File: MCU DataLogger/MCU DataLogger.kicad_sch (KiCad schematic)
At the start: 25 parts, among them U1 24LC1025, U2 DS1337S_, U3 ATMEGA328P-AN, U4 24LC1025, Y1 32.768 KHz, Y2 16MHz

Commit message: MCU Datalogger Project Schematic Complete
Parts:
- U3: footprint ATMEGA328P:QFP80P900X900X120-32N -> ATMEGA328P-AN:QFP80P900X900X120-32N
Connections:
- net VCC: now reaches C1.1
- net VCC: now also R1.1, R2.1, R3.1, R4.1, R6.2, U1.1 (A0), U1.2 (A1), U1.3 (A2), U1.8 (VCC), U2.8 (VCC), U4.1 (A0), U4.3 (A2), U4.8 (VCC)
- net GND: now reaches C1.2
- net GND: now also BT1.2 (-), C2.1, C3.1, C4.1, C5.2, R5.1, R7.2, U1.4 (GND), U1.7 (WP), U2.4 (GND), U3.21 (GND), U3.3 (GND), U3.5 (GND), U4.2 (A1), U4.4 (GND), U4.7 (WP)
- net D3: now reaches U3.1 (PD3)
- net D6: now reaches U3.10 (PD6)
- net D7: now reaches U3.11 (PD7)
- net D8: now reaches U3.12 (PB0)
- net MOSI: now reaches U3.15 (PB3)
- net MISO: now reaches U3.16 (PB4)
- net SCK: now reaches U3.17 (PB5)
- net SCK: now also D1.2 (A), R3.2, U1.6 (SCL), U2.6 (SCL), U3.28 (PC5), U4.6 (SCL)
- net at U3.18 (AVCC): now also BT1.1 (+), C5.1, D2.2 (A), U3.4 (VCC)
- net D4: now reaches U3.2 (PD4)
- net at U3.20 (AREF): now also C4.2
- net SDA: now reaches U3.27 (PC4)
- net SDA: now also R4.2, U1.5 (SDA), U2.5 (SDA), U4.5 (SDA)
- net RESET: now reaches U3.29 (PC6/~{RESET})
- net RESET: now also R6.1
- net RX: now reaches U3.30 (PD0)
- net TX: now reaches U3.31 (PD1)
- net D2: now reaches U3.32 (PD2)
- net at U3.6 (VCC): no longer U3.4 (VCC)
- net at U3.7 (PB6): now also C2.2, Y2.2
- net at U3.8 (PB7): now also C3.2, Y2.1
- net D5: now reaches U3.9 (PD5)
- net at D2.1 (K): now also R7.1
- net at U2.1 (X1): now also Y1.1
- net at U2.2 (X2): now also Y1.2
- net at U2.3 (~{INTA}): now also R1.2
- net at U2.7 (SQW/~INT): now also R2.2
- net at D1.1 (K): now also R5.2
- no-connect marks 0 -> 9
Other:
- sheet Connectors ports: added D2, D3, D4, D5, D6, D7, D8, GND, MISO, MOSI, RESET, RX, SCK, SDA, TX, VCC; removed none
- moved on the sheet: BT1, C1, C2, C3, C4, C5, D1, D2, H1, H2, H3, H4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

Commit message: MCU Datalogger Project 2 Layers V1 Completed
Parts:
- U3: footprint ATMEGA328P-AN:QFP80P900X900X120-32N -> ATMEGA328P:QFP80P900X900X120-32N
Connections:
- net GND: no longer U3.3 (GND), U3.5 (GND)
- net VCC: now also BT1.1 (+), C5.1, D2.2 (A), U3.18 (AVCC), U3.4 (VCC)
- new net: U3.3 (GND), U3.5 (GND)

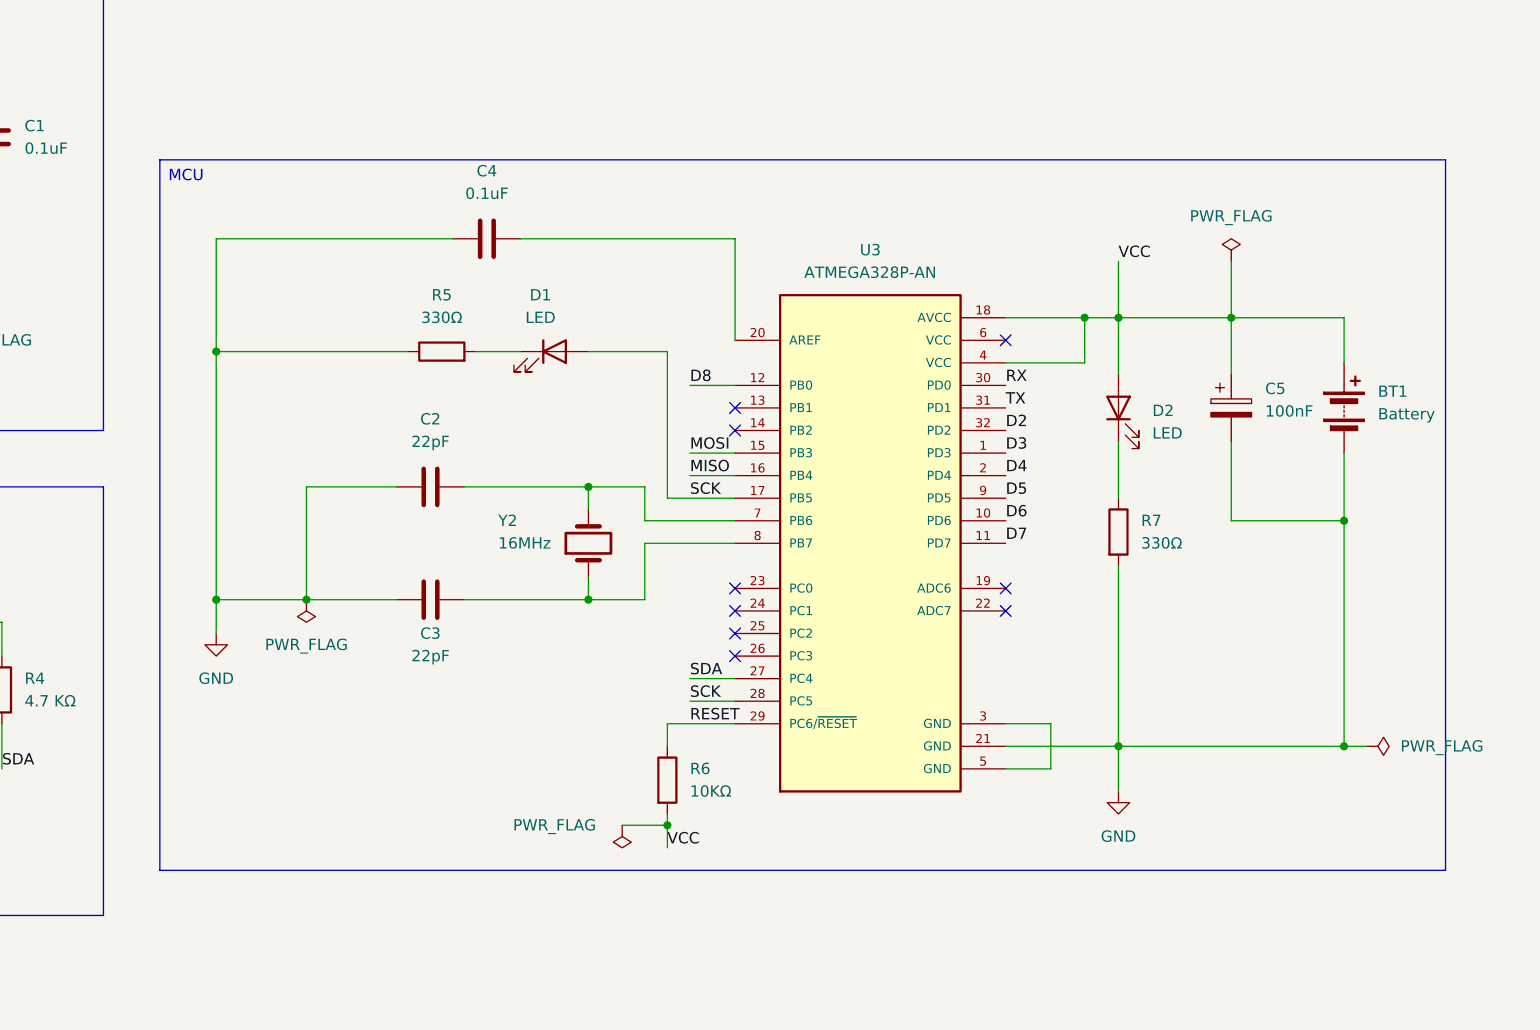
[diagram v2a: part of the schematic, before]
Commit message: MCU DataLogger Enhance 2Layers Version
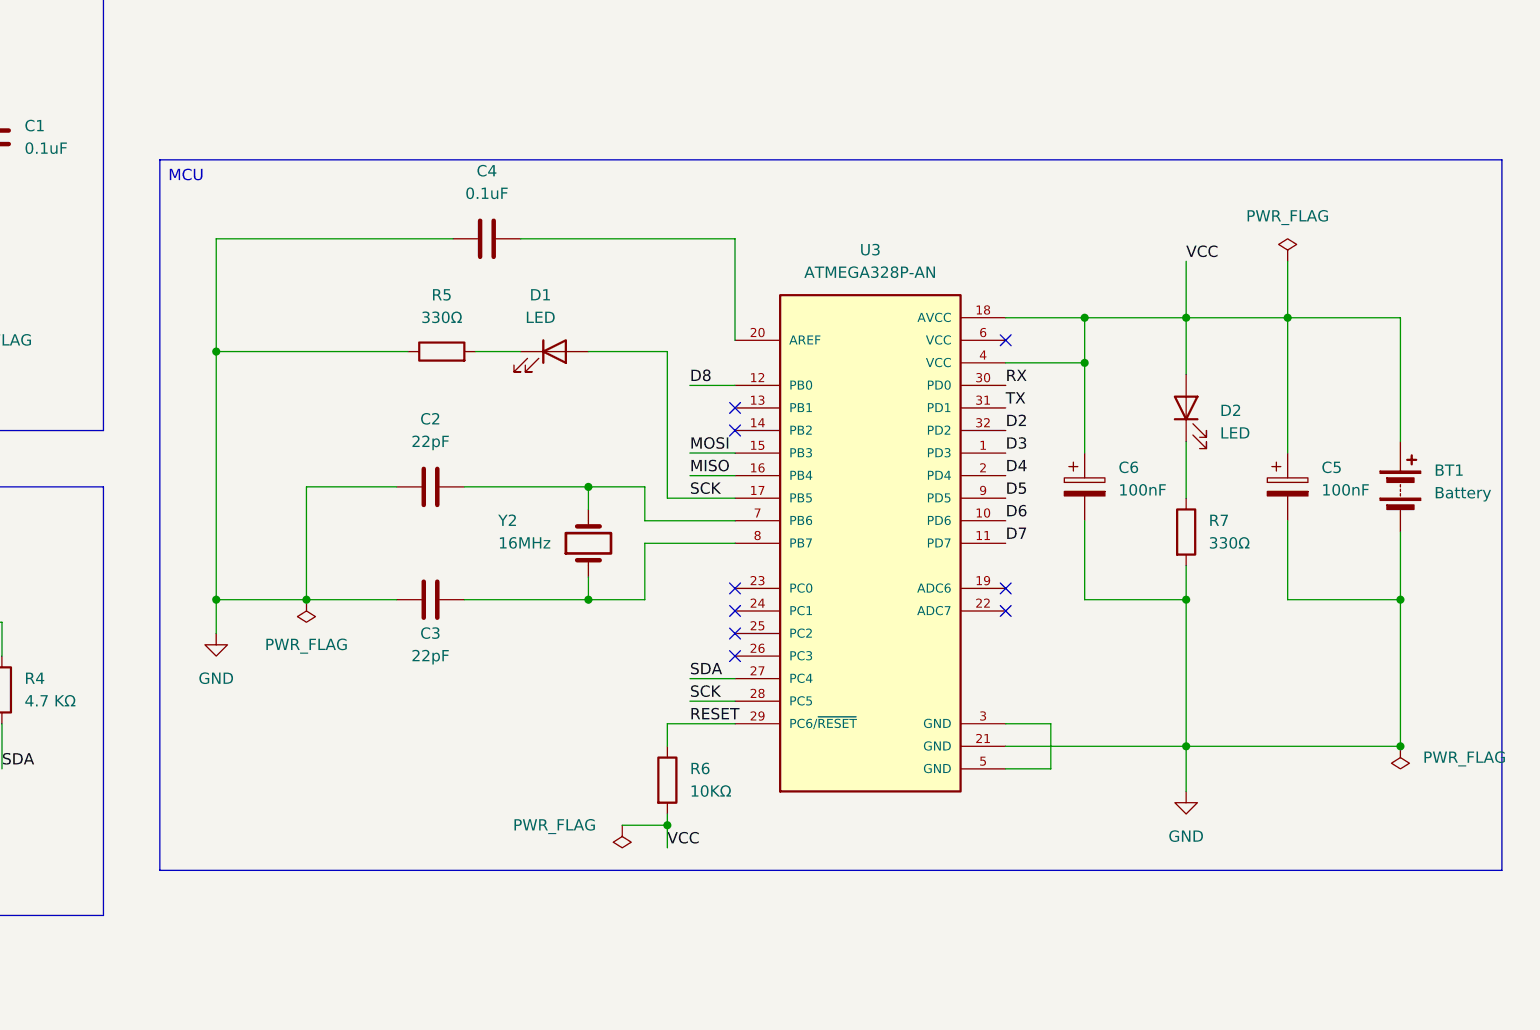
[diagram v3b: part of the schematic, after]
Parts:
- added C6: 100nF, Capacitor_SMD:C_0805_2012Metric, symbol Device:C_Polarized
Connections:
- net GND: now also C6.2
- net VCC: now also C6.1
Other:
- moved on the sheet: BT1, C5, D2, R7
